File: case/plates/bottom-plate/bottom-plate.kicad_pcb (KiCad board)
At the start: 2 copper layers, 140.5 x 112.5 mm, 0 parts

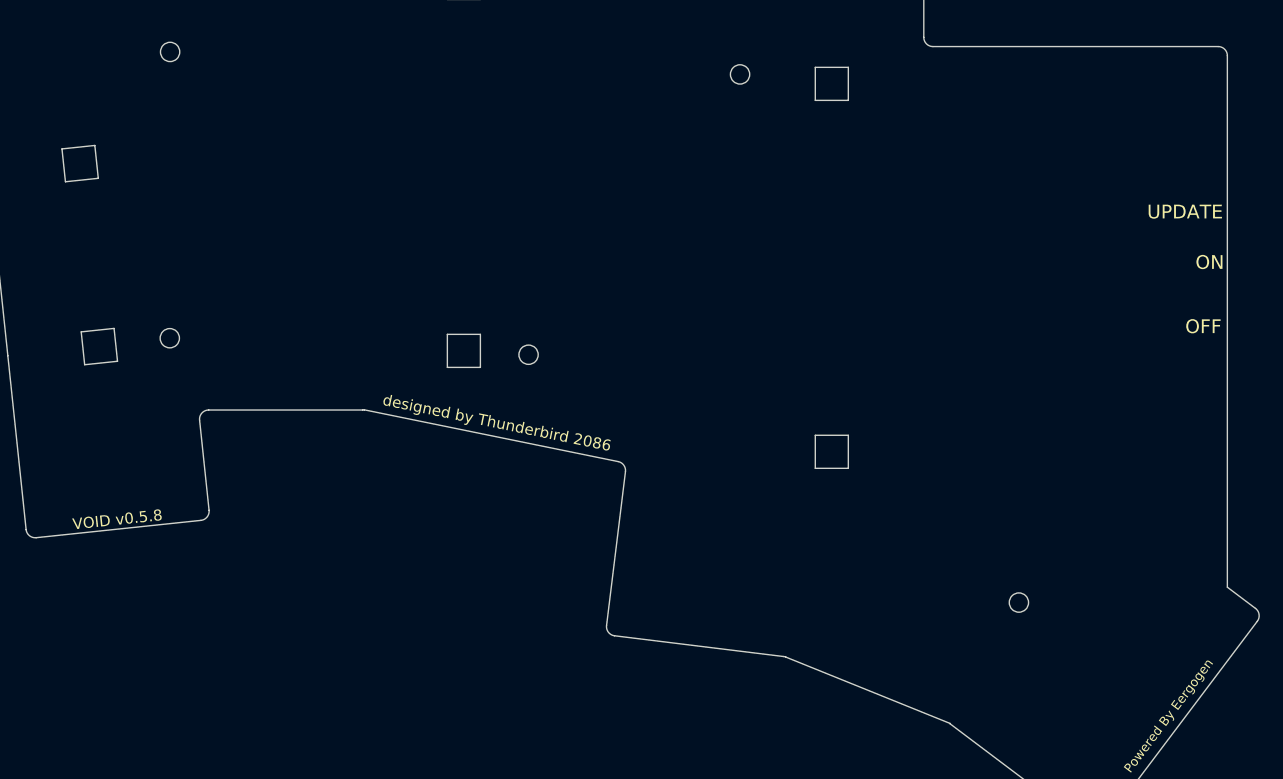
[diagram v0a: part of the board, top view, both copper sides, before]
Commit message: Mcu cover (#7)
* more plates

* updated workflow

* mcu cover

* small change
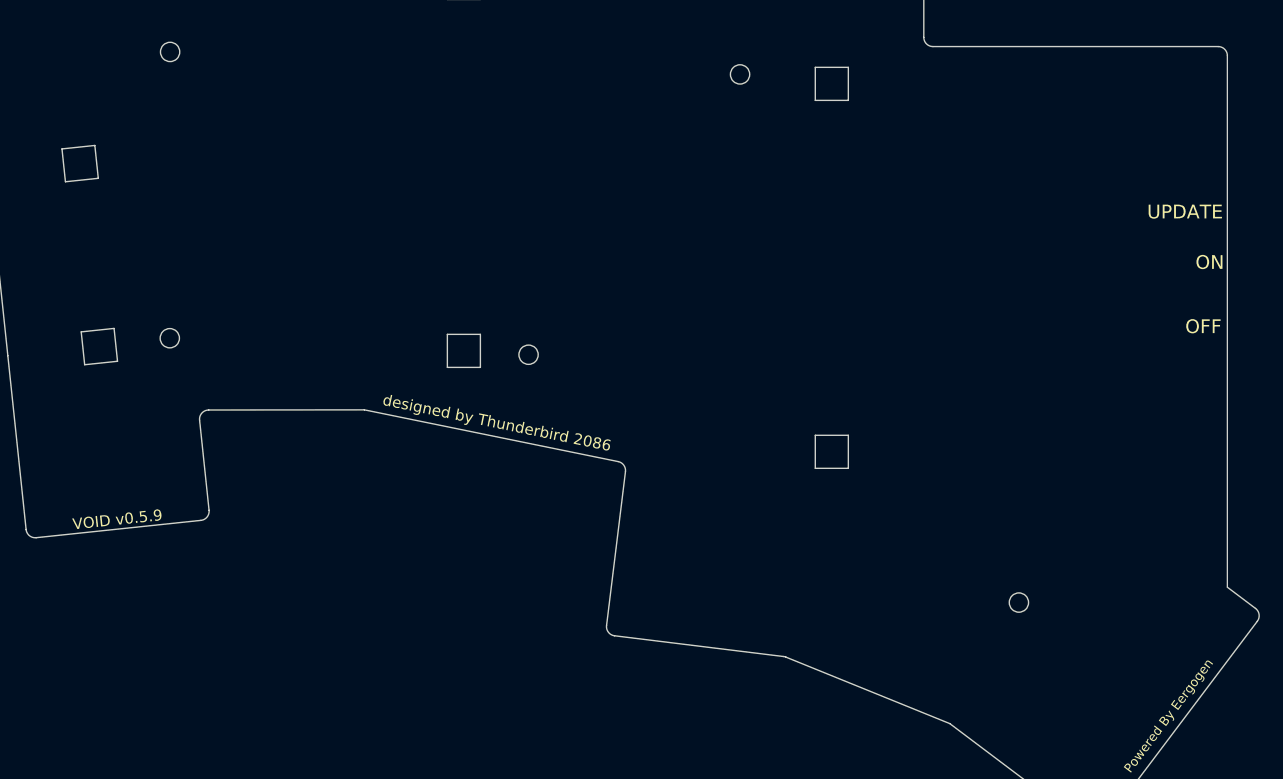
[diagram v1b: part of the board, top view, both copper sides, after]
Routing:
- added copper zone on B.Cu, net (none)
- added copper zone on F.Cu, net (none)
- removed copper zone on B.Cu, net GND
- removed copper zone on F.Cu, net GND
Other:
- outline, holes or cut-outs redrawn
- board text added: "VOID v0.5.9"
- board text removed: "VOID v0.5.8"
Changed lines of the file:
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@@
 	(paper "A4")
 	(title_block
-		(title "bottom-plate")
-		(date "2024-11-10")
-		(rev "0.5.8")
+		(title "VOID Bottom Plate")
+		(date "2024-11-17")
+		(rev "0.5.9")
 		(company "Allen Choi")
 	)
@@
 	)
 	(net 0 "")
-	(net 1 "GND")
 	(gr_line
 		(start 176.034354 115.467322)
@@
 		(layer "Edge.Cuts")
 	)
-	(gr_arc
-		(start 123.293786 112.695167)
-		(mid 123.201968 112.708019)
-		(end 123.109354 112.71232)
-		(stroke
-			(width 0.15)
-			(type default)
-		)
-		(layer "Edge.Cuts")
-	)
 	(gr_line
 		(start 165.209355 57.06232)
@@
 	(gr_line
 		(start 106.326073 112.71232)
-		(end 123.109354 112.71232)
+		(end 123.293786 112.695167)
 		(stroke
 			(width 0.15)
@@
 	)
 	(gr_line
-		(start 217.341854 132.02394)
-		(end 217.341854 74.10232)
-		(stroke
-			(width 0.15)
-			(type default)
-		)
-		(layer "Edge.Cuts")
-	)
-	(gr_line
 		(start 90.710863 87.837382)
 		(end 94.291142 87.461082)
@@
 	)
 	(gr_line
-		(start 169.235269 139.644384)
-		(end 187.114533 146.868073)
+		(start 169.235272 139.644388)
+		(end 187.097266 146.890987)
 		(stroke
 			(width 0.15)
@@
 	)
 	(gr_line
-		(start 187.114533 146.868073)
-		(end 187.097266 146.890987)
-		(stroke
-			(width 0.15)
+		(start 217.341854 74.10232)
+		(end 217.341854 132.02394)
+		(stroke
+			(width 0.05)
 			(type default)
 		)
@@
 	)
 	(gr_arc
-		(start 168.982533 139.579019)
-		(mid 169.111046 139.603407)
-		(end 169.235269 139.644384)
+		(start 168.982533 139.57902)
+		(mid 169.111048 139.603409)
+		(end 169.235272 139.644388)
 		(stroke
 			(width 0.15)
@@
 	(gr_line
 		(start 150.556239 137.316555)
-		(end 168.982533 139.579019)
+		(end 168.982533 139.57902)
 		(stroke
 			(width 0.15)
@@
 		)
 	)
-	(gr_text "VOID v0.5.8"
+	(gr_text "VOID v0.5.9"
 		(at 96.391552 124.665338 6)
 		(layer "B.SilkS")
 		(effects
 			(font
-				(face "Android Robot")
+				(face "ANDROID ROBOT")
 				(size 1.2 1.2)
 				(thickness 0.15)
@@
 			(justify mirror)
 		)
-		(render_cache "VOID v0.5.8" 6
+		(render_cache "VOID v0.5.9" 6
 			(polygon
 				(pts
@@
 			(polygon
 				(pts
-					(xy 92.613857 124.453565) (xy 92.635363 124.460376) (xy 92.687183 124.49268) (xy 92.712623 124.549278)
-					(xy 92.733609 124.748946) (xy 92.7324 124.771124) (xy 92.705323 124.824711) (xy 92.68914 124.838081)
-					(xy 92.642118 124.873456) (xy 92.589786 124.911282) (xy 92.535003 124.950199) (xy 92.483863 124.986173)
-					(xy 92.426222 125.026449) (xy 92.426559 125.029655) (xy 92.671001 125.143064) (xy 92.714301 125.16332)
-					(xy 92.753 125.208645) (xy 92.769364 125.268586) (xy 92.787256 125.438813) (xy 92.777527 125.481175)
-					(xy 92.74535 125.531802) (xy 92.688395 125.555298) (xy 91.826471 125.64589) (xy 91.796985 125.645747)
-					(xy 91.763566 125.631507) (xy 91.720675 125.589577) (xy 91.703208 125.533006) (xy 91.689156 125.399314)
-					(xy 91.934941 125.399314) (xy 92.530738 125.336693) (xy 92.217112 125.187528) (xy 92.2107 125.188202)
-					(xy 91.934941 125.399314) (xy 91.689156 125.399314) (xy 91.686327 125.372397) (xy 91.685361 125.352744)
-					(xy 91.701159 125.294804) (xy 91.723334 125.268118) (xy 91.769951 125.228706) (xy 91.818983 125.190561)
-					(xy 91.867649 125.154049) (xy 91.924707 125.112206) (xy 91.973007 125.077326) (xy 91.97267 125.074119)
-					(xy 91.926637 125.053768) (xy 91.869146 125.027738) (xy 91.812321 124.99814) (xy 91.771959 124.982794)
-					(xy 91.713663 124.955039) (xy 91.661783 124.917676) (xy 91.632989 124.86492) (xy 91.622478 124.764917)
-					(xy 91.858243 124.764917) (xy 92.185322 124.915909) (xy 92.473861 124.700212) (xy 91.858243 124.764917)
-					(xy 91.622478 124.764917) (xy 91.610257 124.648638) (xy 91.618514 124.621026) (xy 91.651714 124.569217)
-					(xy 91.706416 124.545699) (xy 92.585537 124.4533)
+					(xy 92.578833 124.454004) (xy 91.700003 124.546373) (xy 91.644591 124.569966) (xy 91.610833 124.621834)
+					(xy 91.602387 124.649465) (xy 91.603765 124.662582) (xy 91.696716 125.54695) (xy 91.723463 125.603506)
+					(xy 91.769825 125.64085) (xy 91.82035 125.646533) (xy 92.708507 125.553184) (xy 92.764572 125.529523)
+					(xy 92.798738 125.477612) (xy 92.807289 125.449969) (xy 92.773957 125.132833) (xy 92.767253 125.133537)
+					(xy 92.542226 125.157189) (xy 92.54293 125.163893) (xy 92.560761 125.333538) (xy 91.915703 125.401336)
+					(xy 91.855104 124.824777) (xy 91.848915 124.765897) (xy 92.46774 124.700856) (xy 92.158718 124.931967)
+					(xy 92.073896 124.940882) (xy 92.0746 124.947586) (xy 92.098344 125.173488) (xy 92.104756 125.172814)
+					(xy 92.196283 125.163194) (xy 92.256054 125.145531) (xy 92.30899 125.112557) (xy 92.348848 125.078198)
+					(xy 92.406765 125.036694) (xy 92.459525 124.998612) (xy 92.507127 124.963953) (xy 92.562575 124.923065)
+					(xy 92.61899 124.88051) (xy 92.667778 124.841993) (xy 92.700738 124.811931) (xy 92.721261 124.754183)
+					(xy 92.721002 124.724337) (xy 92.704306 124.565477) (xy 92.686694 124.509501) (xy 92.643164 124.46808)
+					(xy 92.609193 124.454055)
 				)
 			)
@@
 		)
 	)
-	(gr_text "VOID v0.5.8"
+	(gr_text "VOID v0.5.9"
 		(at 96.391552 124.665338 6)
 		(layer "F.SilkS")
 		(effects
 			(font
-				(face "Android Robot")
+				(face "ANDROID ROBOT")
 				(size 1.2 1.2)
 				(thickness 0.15)
 			)
 		)
-		(render_cache "VOID v0.5.8" 6
+		(render_cache "VOID v0.5.9" 6
 			(polygon
 				(pts
@@
 			(polygon
 				(pts
-					(xy 101.007828 123.58585) (xy 101.051074 123.629624) (xy 101.064891 123.654916) (xy 101.087624 123.871198)
-					(xy 101.070427 123.928788) (xy 101.02745 123.976121) (xy 100.976198 124.015389) (xy 100.939908 124.038792)
-					(xy 100.890479 124.079558) (xy 100.839656 124.116972) (xy 100.798861 124.146449) (xy 100.799198 124.149655)
-					(xy 100.853694 124.173731) (xy 100.918205 124.202797) (xy 100.973399 124.228393) (xy 101.02929 124.255511)
-					(xy 101.083083 124.284369) (xy 101.110321 124.305861) (xy 101.13782 124.35925) (xy 101.140962 124.378675)
-					(xy 101.157842 124.539284) (xy 101.152519 124.59825) (xy 101.119283 124.648182) (xy 101.089554 124.669059)
-					(xy 101.060742 124.675329) (xy 100.198819 124.765921) (xy 100.138223 124.75478) (xy 100.096223 124.711949)
-					(xy 100.077899 124.672536) (xy 100.061795 124.519314) (xy 100.30758 124.519314) (xy 100.903377 124.456693)
-					(xy 100.589751 124.307529) (xy 100.583339 124.308203) (xy 100.30758 124.519314) (xy 100.061795 124.519314)
-					(xy 100.060008 124.502308) (xy 100.063552 124.440276) (xy 100.091981 124.387894) (xy 100.130124 124.359079)
-					(xy 100.345646 124.197326) (xy 100.345309 124.194119) (xy 100.280553 124.166707) (xy 100.223051 124.142152)
-					(xy 100.161374 124.115476) (xy 100.102321 124.089357) (xy 100.048972 124.064531) (xy 100.030362 124.054819)
-					(xy 99.992736 124.008032) (xy 99.986942 123.98659) (xy 99.976256 123.884917) (xy 100.230882 123.884917)
-					(xy 100.557961 124.035909) (xy 100.8465 123.820213) (xy 100.230882 123.884917) (xy 99.976256 123.884917)
-					(xy 99.965957 123.786922) (xy 99.979073 123.726271) (xy 100.023044 123.683899) (xy 100.042665 123.672766)
-					(xy 100.07031 123.666618) (xy 100.949432 123.574219)
+					(xy 100.077014 123.665914) (xy 100.955844 123.573545) (xy 101.01495 123.585101) (xy 101.058755 123.628817)
+					(xy 101.072761 123.654089) (xy 101.07414 123.667206) (xy 101.167091 124.551574) (xy 101.152688 124.612455)
+					(xy 101.115102 124.658622) (xy 101.066863 124.674686) (xy 100.178706 124.768035) (xy 100.118947 124.756547)
+					(xy 100.074735 124.712874) (xy 100.060623 124.687613) (xy 100.027291 124.370477) (xy 100.033995 124.369772)
+					(xy 100.259022 124.346121) (xy 100.259726 124.352825) (xy 100.277557 124.52247) (xy 100.922615 124.454671)
+					(xy 100.862016 123.878112) (xy 100.855828 123.819232) (xy 100.237003 123.884273) (xy 100.587323 124.046085)
+					(xy 100.672145 124.03717) (xy 100.67285 124.043874) (xy 100.696593 124.269776) (xy 100.69018 124.27045)
+					(xy 100.598654 124.280069) (xy 100.536516 124.275219) (xy 100.477881 124.253972) (xy 100.43175 124.22865)
+					(xy 100.36647 124.200095) (xy 100.306945 124.173815) (xy 100.253177 124.149811) (xy 100.190441 124.121344)
+					(xy 100.12641 124.091448) (xy 100.07068 124.063916) (xy 100.03219 124.041365) (xy 100.000109 123.989145)
+					(xy 99.994157 123.959898) (xy 99.97746 123.801038) (xy 99.983049 123.742624) (xy 100.017015 123.693057)
+					(xy 100.047328 123.672275)
 				)
 			)
@@
 	)
 	(zone
-		(net 1)
-		(net_name "GND")
+		(net 0)
+		(net_name "")
 		(layers "F&B.Cu")
 		(hatch edge 0.5)
 		(connect_pads yes
-			(clearance 0.508)
-		)
-		(min_thickness 0.25)
+			(clearance 0.1)
+		)
+		(min_thickness 0.1)
 		(filled_areas_thickness no)
 		(fill yes
-			(thermal_gap 0.5)
-			(thermal_bridge_width 0.5)
+			(mode hatch)
+			(thermal_gap 0.1)
+			(thermal_bridge_width 0.1)
 			(smoothing chamfer)
 			(radius 0.5)
 			(island_removal_mode 1)
 			(island_area_min 5)
+			(hatch_thickness 0.5)
+			(hatch_gap 1.5)
+			(hatch_orientation 60)
+			(hatch_border_algorithm hatch_thickness)
+			(hatch_min_hole_area 0.3)
 		)
 		(polygon

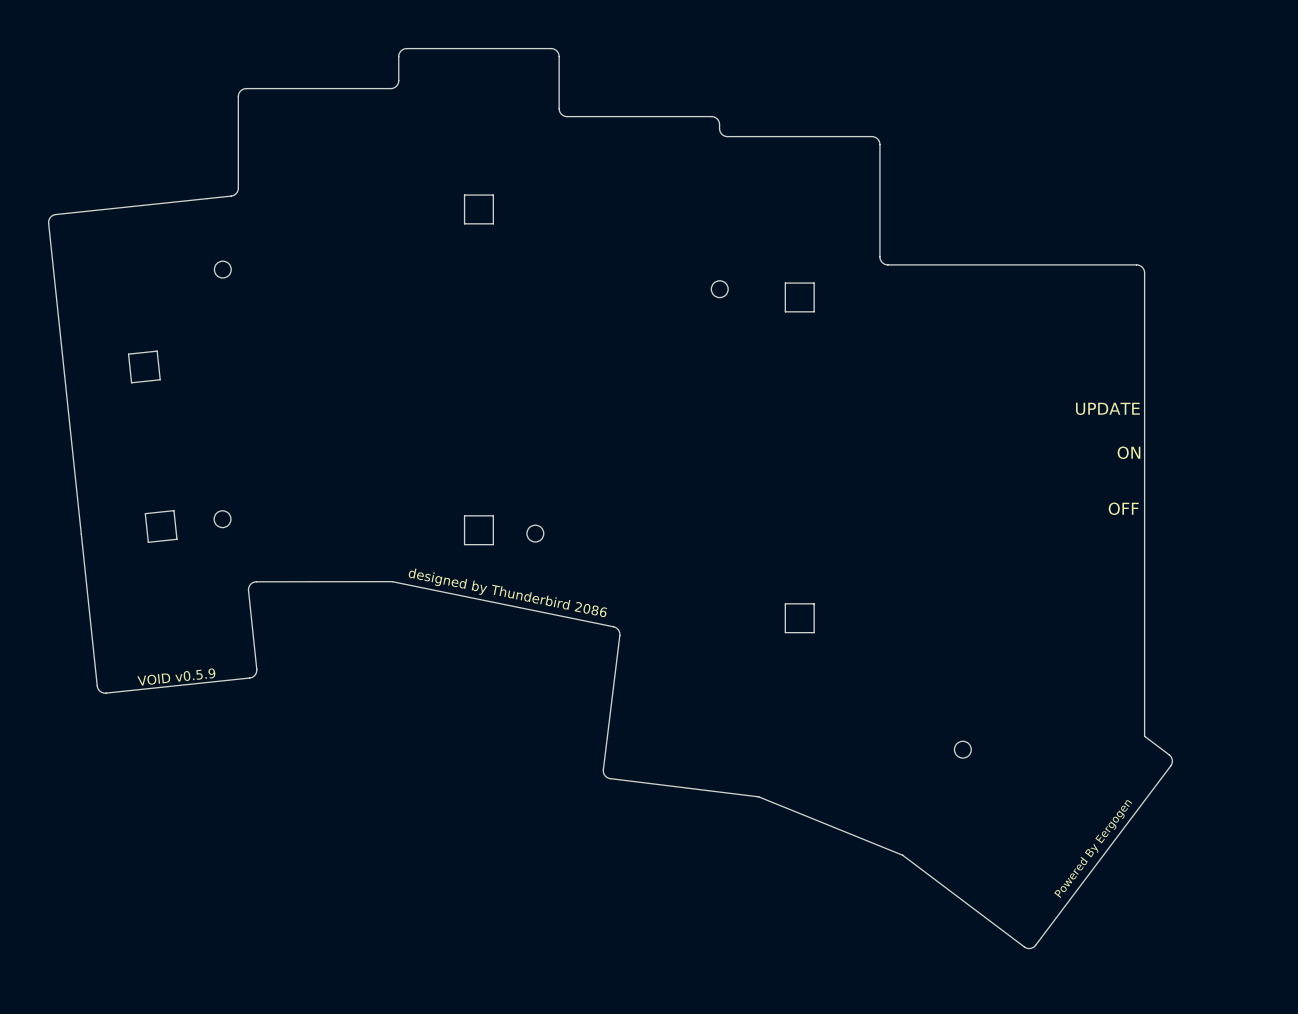
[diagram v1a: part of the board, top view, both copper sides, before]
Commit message: Changed TRRS to USB-C connector (#14)
* usb-c mod for hybrid

* updated
  - submodule
  - ergogen yaml
  - schematic and pcb

* updated cherry-mx

usb-c for communication between left and right hand sides

* updated choc

* updated choc

* fixed corner

* void-choc

* ergogen
  - bottom plate
  - charger plate

* updated choc

* updated ergogen

* cherry-mx
* hybrid-mx

* updated ergogen for VOID Choc

* refreshed submodule

* updated ergogen yaml

* updated PCBs

* updated version
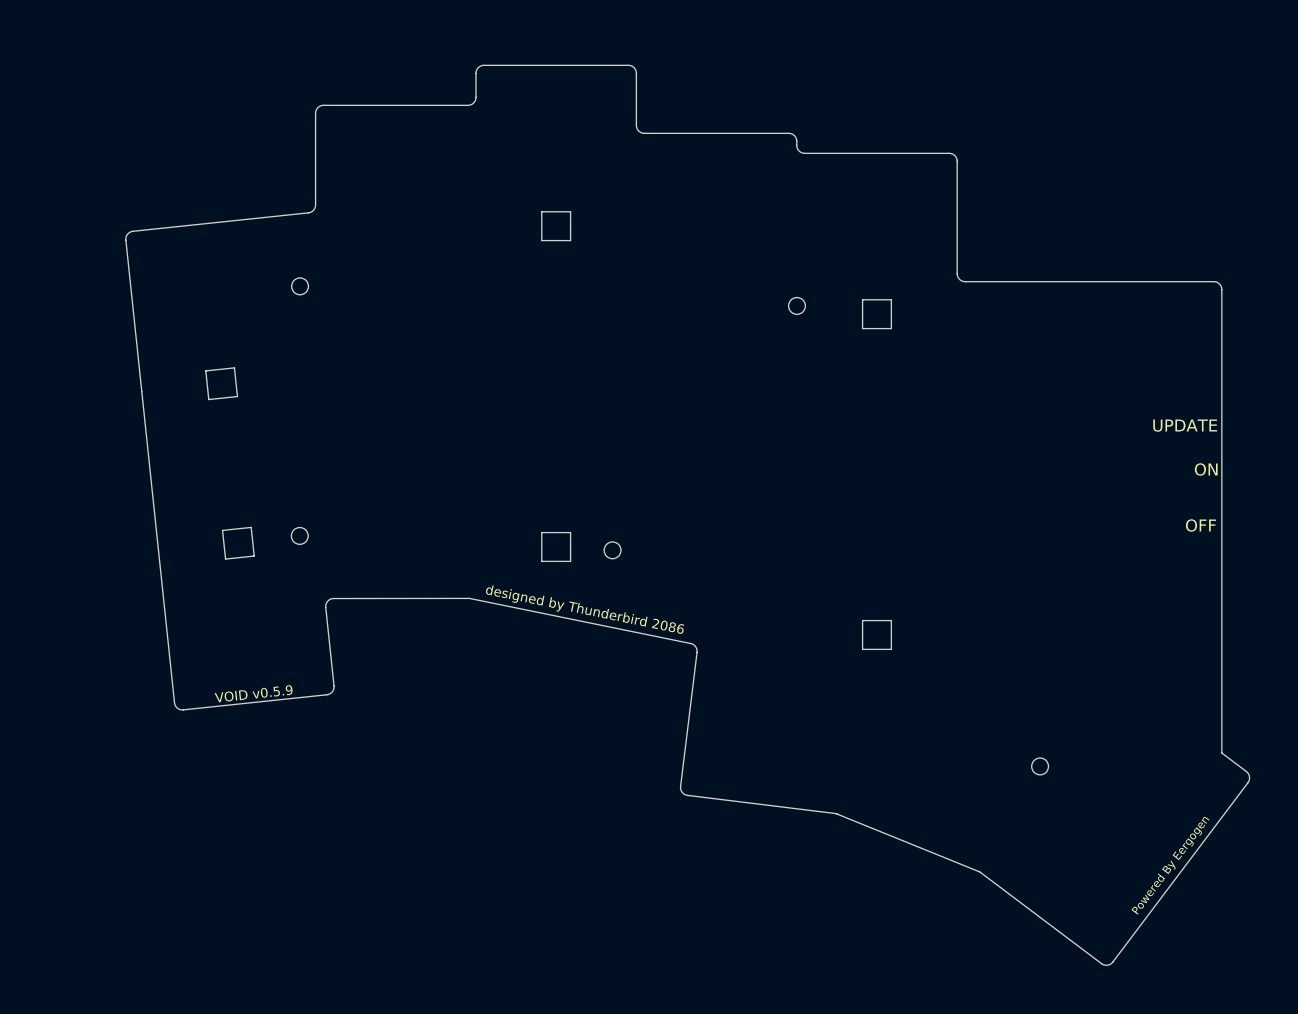
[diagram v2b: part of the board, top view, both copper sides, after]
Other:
- board text added: "offset: 90, 70 from origin"
